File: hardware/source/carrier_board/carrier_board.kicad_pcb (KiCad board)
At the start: 2 copper layers, 60 x 38 mm, 17 parts, among them J1 12V_IN, J2 LIPO_BAT, J3 LUCKFOX_J1, J4 LUCKFOX_J2, J5 SC3336_FPC, J7 USB_WIFI, SW1 PWR_BTN, U1 LM2596_BUCK, U2 IP5306_BMS

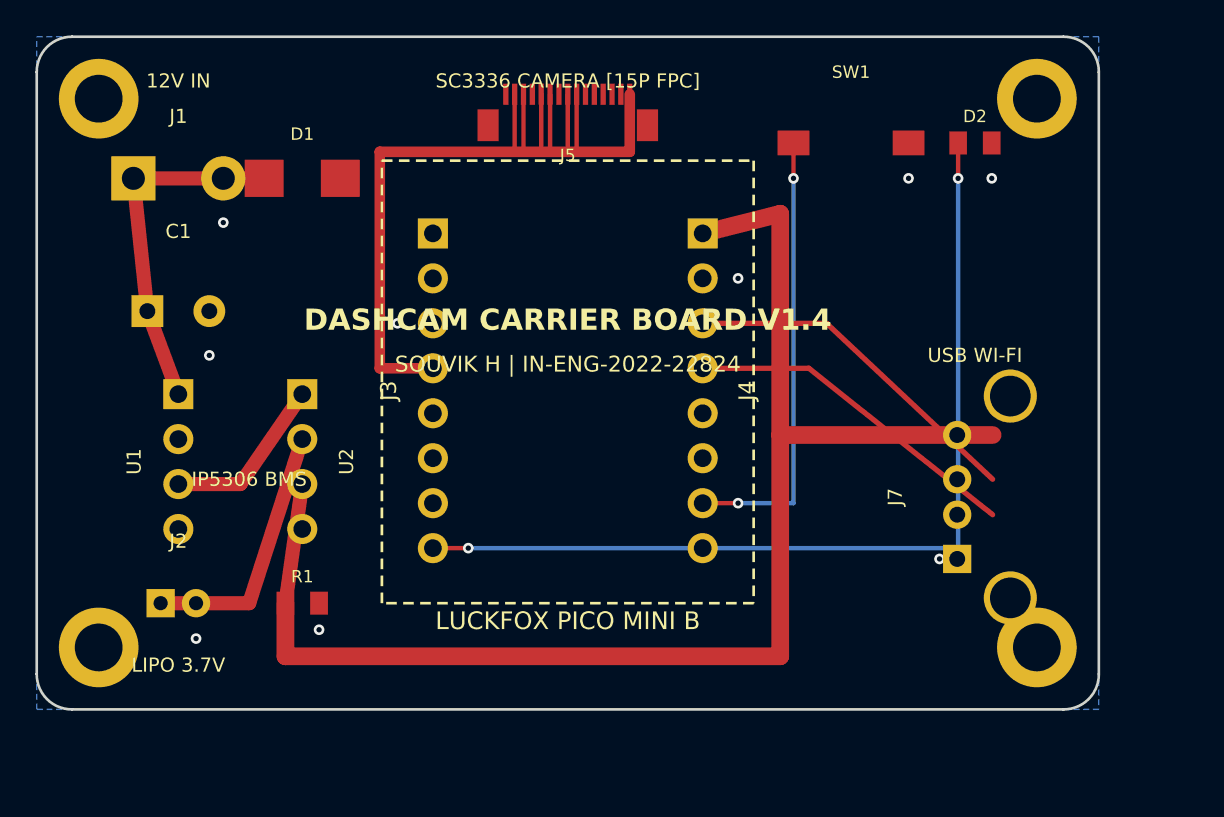
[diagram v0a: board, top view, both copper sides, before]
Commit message: hardware(carrier_board): complete 100% autorouting via Freerouting with zero DRC errors and export production artifacts
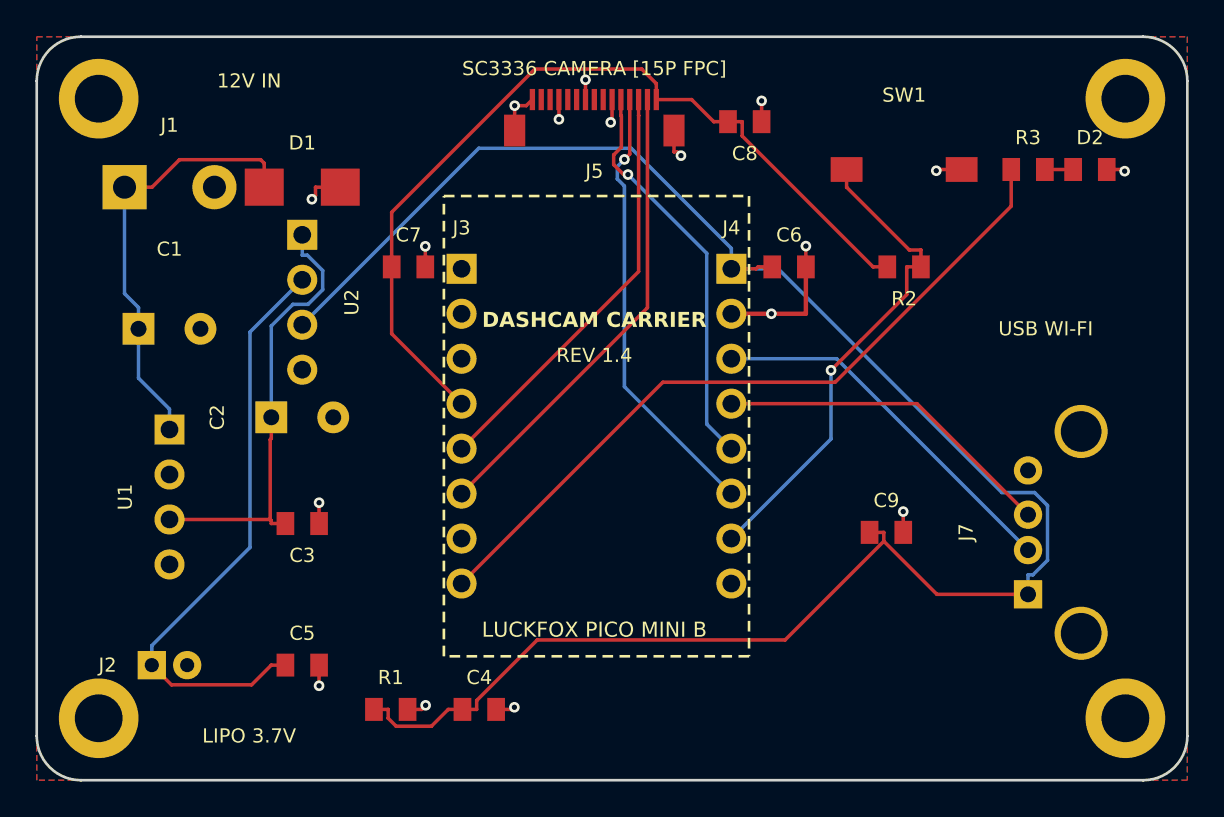
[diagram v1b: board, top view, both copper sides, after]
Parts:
- removed the ? at (156.5, 83.5)
- removed the ? at (103.5, 114.5)
- removed the ? at (156.5, 114.5)
- added ?: , MountingHole:MountingHole_2.7mm_M2.5_Pad, F.Cu at (103.5, 118.5)
- added ?: , MountingHole:MountingHole_2.7mm_M2.5_Pad, F.Cu at (161.5, 118.5)
- added ?: , MountingHole:MountingHole_2.7mm_M2.5_Pad, F.Cu at (161.5, 83.5)
- added C2: 470uF, Capacitor_THT:CP_Radial_D8.0mm_P3.50mm, F.Cu at (115.0, 101.5)
- added C3: 100nF, Capacitor_SMD:C_0805_2012Metric, F.Cu at (115.0, 107.5)
- added C4: 100nF, Capacitor_SMD:C_0805_2012Metric, F.Cu at (125.0, 118.0)
- added C5: 100nF, Capacitor_SMD:C_0805_2012Metric, F.Cu at (115.0, 115.5)
- added C6: 100nF, Capacitor_SMD:C_0805_2012Metric, F.Cu at (142.5, 93.0)
- added C7: 100nF, Capacitor_SMD:C_0805_2012Metric, F.Cu at (121.0, 93.0)
- added C8: 100nF, Capacitor_SMD:C_0805_2012Metric, F.Cu at (140.0, 84.8)
- added C9: 100nF, Capacitor_SMD:C_0805_2012Metric, F.Cu at (148.0, 108.0)
- added R2: 10k, Resistor_SMD:R_0805_2012Metric, F.Cu at (149.0, 93.0)
- added R3: 470R, Resistor_SMD:R_0805_2012Metric, F.Cu at (156.0, 87.5)
- moved U2 9.00 mm to (115.0, 95.0)
- moved R1 7.81 mm to (120.0, 118.0)
- moved D2 6.67 mm to (159.5, 87.5)
- moved J7 4.47 mm to (157.0, 108.0)
- moved J2 3.54 mm to (107.5, 115.5)
- moved SW1 3.35 mm to (149.0, 87.5)
- moved J3 2.57 mm to (124.0, 102.0)
- moved J4 2.57 mm to (139.2, 102.0)
- moved U1 2.06 mm to (107.5, 106.0)
- moved J5 1.53 mm to (131.5, 84.8)
- moved C1 1.12 mm to (107.5, 96.5)
- moved J1 0.71 mm to (107.5, 88.5)
- moved D1 0.50 mm to (115.0, 88.5)
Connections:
- net +12V_IN renamed +12V
- D2 pad 1: STAT_LED -> Net-(D2-A)
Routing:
- net +5V_SYS: track 79.3 -> 108.1 mm
- net GND: track 0.00 -> 28.6 mm, vias 9 -> 17
- net I2C3_SDA: track 0.00 -> 26.6 mm
- net CAM_PDN: track 0.00 -> 25.2 mm, vias 0 -> 1
- net I2C3_SCL: track 0.00 -> 23.9 mm
- net CAM_RSTn: track 0.00 -> 22.8 mm, vias 0 -> 1
- net VBAT: track 14.7 -> 33.8 mm
- net +3V3: track 32.6 -> 49.4 mm
- net +5V_PRE: track 9.67 -> 25.2 mm
- net STAT_LED: track 52.6 -> 42.0 mm, vias 2 -> 0
- net +12V: track 19.9 -> 24.7 mm
- net MIPI_D1_P: track 3.25 -> 0.00 mm
- net MIPI_D1_N: track 3.25 -> 0.00 mm
- net MIPI_D0_P: track 3.25 -> 0.00 mm
- net MIPI_D0_N: track 3.25 -> 0.00 mm
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- added copper zone on F.Cu, net GND
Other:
- board size 60 x 38 mm -> 65 x 42 mm
- board text added: "DASHCAM CARRIER"
- board text added: "REV 1.4"
- board text removed: "IP5306 BMS"
